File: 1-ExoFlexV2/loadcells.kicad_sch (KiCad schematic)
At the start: 50 parts, among them J70 3,3k, J71 3,3k, J72 0Ω, J73 0Ω, J74 0Ω, J75 0Ω, U13 INA823DR, U14 INA823DR, U15 INA823DR, U19 SN74LVC1G32DBVR, U20 SN74LVC1G32DBVR

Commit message: Schématisation terminée
- Schéma terminé
- Passage vers le PCB
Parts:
- C22, C23, C24, C25, C26, C27: renamed from C?; value * -> 10nF 10V X5R; footprint Capacitor_SMD:C_0805_2012Metric -> Capacitor_SMD:C_01005_0402Metric; DESCRIPTION (none) -> 10000 pF ±10% 10V Ceramic Capacitor X5R 01005 (0402 Metric); MANUFACTURER (none) -> Murata Electronics; NOTES (none) -> DO NOT POPULATE; PACKAGE (none) -> 01005 (0402 Metric); PART NUMBER (none) -> GRM022R61A103KE19L; TYPE (none) -> SMD
- J74: renamed from J70; value 3,3k -> Tulip Conn; footprint Connector_PinHeader_2.54mm:PinHeader_1x02_P2.54mm_Vertical -> Connector_PinSocket_2.54mm:PinSocket_1x02_P2.54mm_Vertical; DESCRIPTION (none) -> 2 Position Socket Connector 0.100" (2.54mm) Through Hole Go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; MANUFACTURER (none) -> Preci-Dip; PACKAGE (none) -> 2 POS 0.100" (2.54mm); PART NUMBER (none) -> 801-87-002-10-001101; TYPE (none) -> Through Hole
- J75: renamed from J71; value 3,3k -> Tulip Conn; footprint Connector_PinHeader_2.54mm:PinHeader_1x02_P2.54mm_Vertical -> Connector_PinSocket_2.54mm:PinSocket_1x02_P2.54mm_Vertical; DESCRIPTION (none) -> 2 Position Socket Connector 0.100" (2.54mm) Through Hole Go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; MANUFACTURER (none) -> Preci-Dip; PACKAGE (none) -> 2 POS 0.100" (2.54mm); PART NUMBER (none) -> 801-87-002-10-001101; TYPE (none) -> Through Hole
- J76: renamed from J72; value 0Ω -> Tulip Conn; footprint Connector_PinHeader_2.54mm:PinHeader_1x02_P2.54mm_Vertical -> Connector_PinSocket_2.54mm:PinSocket_1x02_P2.54mm_Vertical; DESCRIPTION (none) -> 2 Position Socket Connector 0.100" (2.54mm) Through Hole Go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; MANUFACTURER (none) -> Preci-Dip; PACKAGE (none) -> 2 POS 0.100" (2.54mm); PART NUMBER (none) -> 801-87-002-10-001101; TYPE (none) -> Through Hole
- J77: renamed from J73; value 0Ω -> Tulip Conn; footprint Connector_PinHeader_2.54mm:PinHeader_1x02_P2.54mm_Vertical -> Connector_PinSocket_2.54mm:PinSocket_1x02_P2.54mm_Vertical; DESCRIPTION (none) -> 2 Position Socket Connector 0.100" (2.54mm) Through Hole Go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; MANUFACTURER (none) -> Preci-Dip; PACKAGE (none) -> 2 POS 0.100" (2.54mm); PART NUMBER (none) -> 801-87-002-10-001101; TYPE (none) -> Through Hole
- J78: renamed from J74; value 0Ω -> Tulip Conn; footprint Connector_PinHeader_2.54mm:PinHeader_1x02_P2.54mm_Vertical -> Connector_PinSocket_2.54mm:PinSocket_1x02_P2.54mm_Vertical; DESCRIPTION (none) -> 2 Position Socket Connector 0.100" (2.54mm) Through Hole Go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; MANUFACTURER (none) -> Preci-Dip; PACKAGE (none) -> 2 POS 0.100" (2.54mm); PART NUMBER (none) -> 801-87-002-10-001101; TYPE (none) -> Through Hole
- J79: renamed from J75; value 0Ω -> Tulip Conn; footprint Connector_PinHeader_2.54mm:PinHeader_1x02_P2.54mm_Vertical -> Connector_PinSocket_2.54mm:PinSocket_1x02_P2.54mm_Vertical; DESCRIPTION (none) -> 2 Position Socket Connector 0.100" (2.54mm) Through Hole Go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; MANUFACTURER (none) -> Preci-Dip; PACKAGE (none) -> 2 POS 0.100" (2.54mm); PART NUMBER (none) -> 801-87-002-10-001101; TYPE (none) -> Through Hole
- J80, J81, J82, J83, J84, J85: renamed from J?; value Jmp -> Jumper; footprint (none) -> Connector_PinSocket_2.54mm:PinSocket_1x03_P2.54mm_Vertical; DESCRIPTION (none) -> CONN HEADER VERT 3POS 2.54MM; MANUFACTURER (none) -> Würth Elektronik; PACKAGE (none) -> Square 0.100" (2.54mm); PART NUMBER (none) -> 61300311121; TYPE (none) -> Through Hole
- R59: renamed from R37; value 910k -> 910k 0,1% 1/8W; DESCRIPTION (none) -> 910 kOhms ±0.1% 0.125W, 1/8W Chip Resistor 0805 (2012 Metri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; MANUFACTURER (none) -> Panasonic Electronic Components; PACKAGE (none) -> 0805 (2012 Metric); PART NUMBER (none) -> ERA-6AEB914V; TYPE (none) -> SMD
- R60, R66: renamed from R?; value 910k -> 910k 0,1% 1/8W; DESCRIPTION (none) -> 910 kOhms ±0.1% 0.125W, 1/8W Chip Resistor 0805 (2012 Metri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; MANUFACTURER (none) -> Panasonic Electronic Components; PACKAGE (none) -> 0805 (2012 Metric); PART NUMBER (none) -> ERA-6AEB914V; TYPE (none) -> SMD
- R61, R62, R63, R64, R65, R67: renamed from R?; DESCRIPTION (none) -> 0 Ohms Jumper Chip Resistor 0805 (2012 Metric) Automotive A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; MANUFACTURER (none) -> Panasonic Electronic Components; PACKAGE (none) -> 0805 (2012 Metric); PART NUMBER (none) -> ERJ-6GEY0R00V; TYPE (none) -> SMD
- R68, R69, R70: renamed from R?; value 1k -> 1k 1% 1/10W; footprint Resistor_SMD:R_0805_2012Metric -> Resistor_SMD:R_0402_1005Metric; DESCRIPTION (none) -> 1 kOhms ±1% 0.1W, 1/10W Chip Resistor 0402 (1005 Metric) Au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; MANUFACTURER (none) -> Panasonic Electronic Components; PACKAGE (none) -> 0402 (1005 Metric); PART NUMBER (none) -> ERJ-2RKF1001X; TYPE (none) -> SMD
- R71, R72, R73, R74, R75, R76: renamed from R?; value 100k -> 100k 5% 1/8W; DESCRIPTION (none) -> 100 kOhms ±5% 0.125W, 1/8W Chip Resistor 0805 (2012 Metric)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; MANUFACTURER (none) -> Panasonic Electronic Components; PACKAGE (none) -> 0805 (2012 Metric); PART NUMBER (none) -> ERJ-6GEYJ104V; TYPE (none) -> SMD
- RV15: renamed from RV1; value 402Ω -> Trim 1k; DESCRIPTION (none) -> Trimmer 1k 0,5W PC PIN TOP; MANUFACTURER (none) -> Bourns Inc.; PACKAGE (none) -> Rectangular - 0.275" x 0.260" Face; PART NUMBER (none) -> 3362P-1-102LF; TYPE (none) -> Through Hole
- RV16: renamed from RV2; value 402Ω -> Trim 1k; DESCRIPTION (none) -> Trimmer 1k 0,5W PC PIN TOP; MANUFACTURER (none) -> Bourns Inc.; PACKAGE (none) -> Rectangular - 0.275" x 0.260" Face; PART NUMBER (none) -> 3362P-1-102LF; TYPE (none) -> Through Hole
- RV17: renamed from RV3; value 402Ω -> Trim 1k; DESCRIPTION (none) -> Trimmer 1k 0,5W PC PIN TOP; MANUFACTURER (none) -> Bourns Inc.; PACKAGE (none) -> Rectangular - 0.275" x 0.260" Face; PART NUMBER (none) -> 3362P-1-102LF; TYPE (none) -> Through Hole
- RV18, RV19, RV20: renamed from RV?; value 523Ω -> Trim 1k; DESCRIPTION (none) -> Trimmer 1k 0,5W PC PIN TOP; MANUFACTURER (none) -> Bourns Inc.; PACKAGE (none) -> Rectangular - 0.275" x 0.260" Face; PART NUMBER (none) -> 3362P-1-102LF; TYPE (none) -> Through Hole
- U25: renamed from U13; value INA823DR -> INST OP-AMP; DESCRIPTION (none) -> Instrumentation Amplifier 1 Circuit 8-SOIC; MANUFACTURER (none) -> Texas Instruments; PACKAGE (none) -> 8-SOIC (0.154", 3.90mm Width); PART NUMBER (none) -> INA823DR; TYPE (none) -> SMD
- U26: renamed from U14; value INA823DR -> INST OP-AMP; DESCRIPTION (none) -> Instrumentation Amplifier 1 Circuit 8-SOIC; MANUFACTURER (none) -> Texas Instruments; PACKAGE (none) -> 8-SOIC (0.154", 3.90mm Width); PART NUMBER (none) -> INA823DR; TYPE (none) -> SMD
- U27: renamed from U15; value INA823DR -> INST OP-AMP; DESCRIPTION (none) -> Instrumentation Amplifier 1 Circuit 8-SOIC; MANUFACTURER (none) -> Texas Instruments; PACKAGE (none) -> 8-SOIC (0.154", 3.90mm Width); PART NUMBER (none) -> INA823DR; TYPE (none) -> SMD
- U28, U29, U30: renamed from U?; value LM393DGKR -> COMP; footprint DGK8 -> FootPrint:DGK8; DESCRIPTION (none) -> Comparator General Purpose Open-Collector, Rail-to-Rail 8-V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; MANUFACTURER (none) -> Texas Instruments; PACKAGE (none) -> 8-TSSOP, 8-MSOP (0.118", 3.00mm Width); PART NUMBER (none) -> LM393DGKR; TYPE (none) -> SMD
- U31: renamed from U19; value SN74LVC1G32DBVR -> OR Gate; DESCRIPTION (none) -> OR Gate IC 1 Channel SOT-23-5; MANUFACTURER (none) -> Texas Instruments; PACKAGE (none) -> SC-74A, SOT-753; PART NUMBER (none) -> SN74LVC1G32DBVR; TYPE (none) -> SMD
- U32: renamed from U20; value SN74LVC1G32DBVR -> OR Gate; DESCRIPTION (none) -> OR Gate IC 1 Channel SOT-23-5; MANUFACTURER (none) -> Texas Instruments; PACKAGE (none) -> SC-74A, SOT-753; PART NUMBER (none) -> SN74LVC1G32DBVR; TYPE (none) -> SMD
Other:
- note added: "3,3kΩ"
- note added: "3xComp : 5VA @ 77,4mA 2xOrGate : 5V @ 64,02mA 3xPot10k : 5VA @ 30mA 3xLimit : 5VA @ 60mA 3x910k : 5VA @ 0,016mA 6x100k : 5VA @ 0,3mA 3xPot523 : 5VA @ 30mA 3xAmInst : ±5VA @ 150,9 Total current : 5V @ 69mA 5VA @ 357mA -5VA @ 150,9mA"
- note added: "402Ω"
- note added: "523Ω"
- note removed: "3xComp : 5VA @ 24,5mA 2xOrGate : 5V @ 64,02mA 3xInstAmp : ±5VA @ 150,9mA 3xPot10k : 5VA @ 1,5mA 3xLim10,2k : 5VA @ 1,47mA 3x200k : 5V @ 0,075mA 3x910k: 5VA @ 0,016mA Total current : 5VA @ 180mA -5VA @ 152mA 5V @150,02mA"
- moved on the sheet: C22, C26, C27, J78, J79, J83, R61, R66, R67, R73

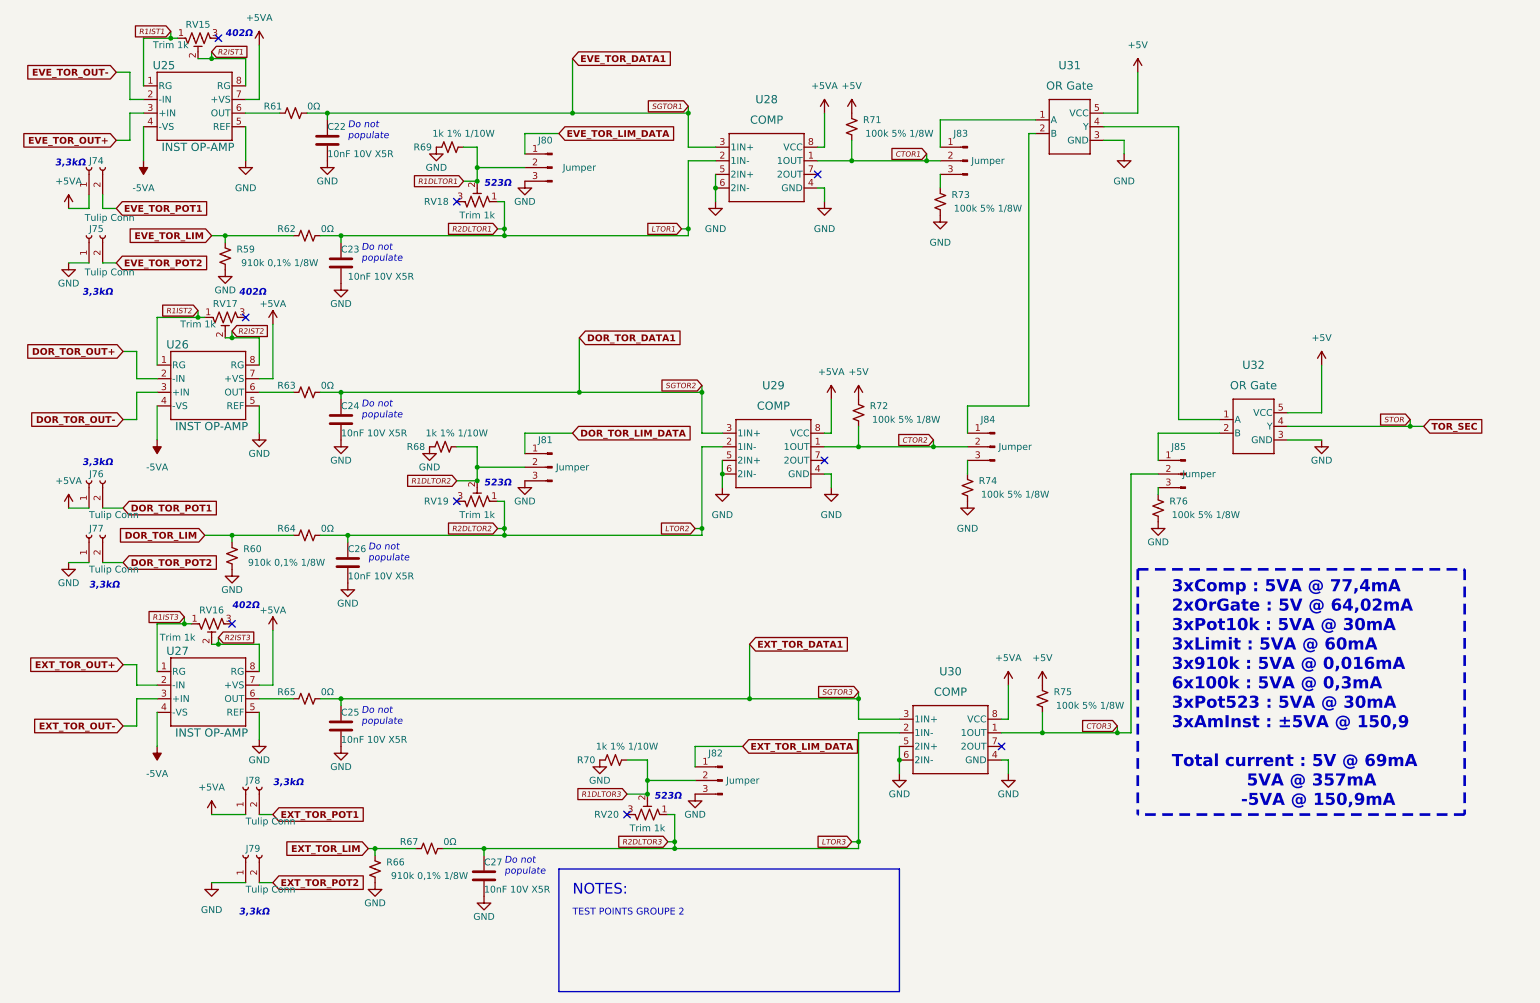
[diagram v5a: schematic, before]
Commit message: Finalisation 3
- Changement des régulateur de tension
- Retrait de test point inutile
- Changement de jumper mal positionner
- Ajout de Mounting holes et fiducial
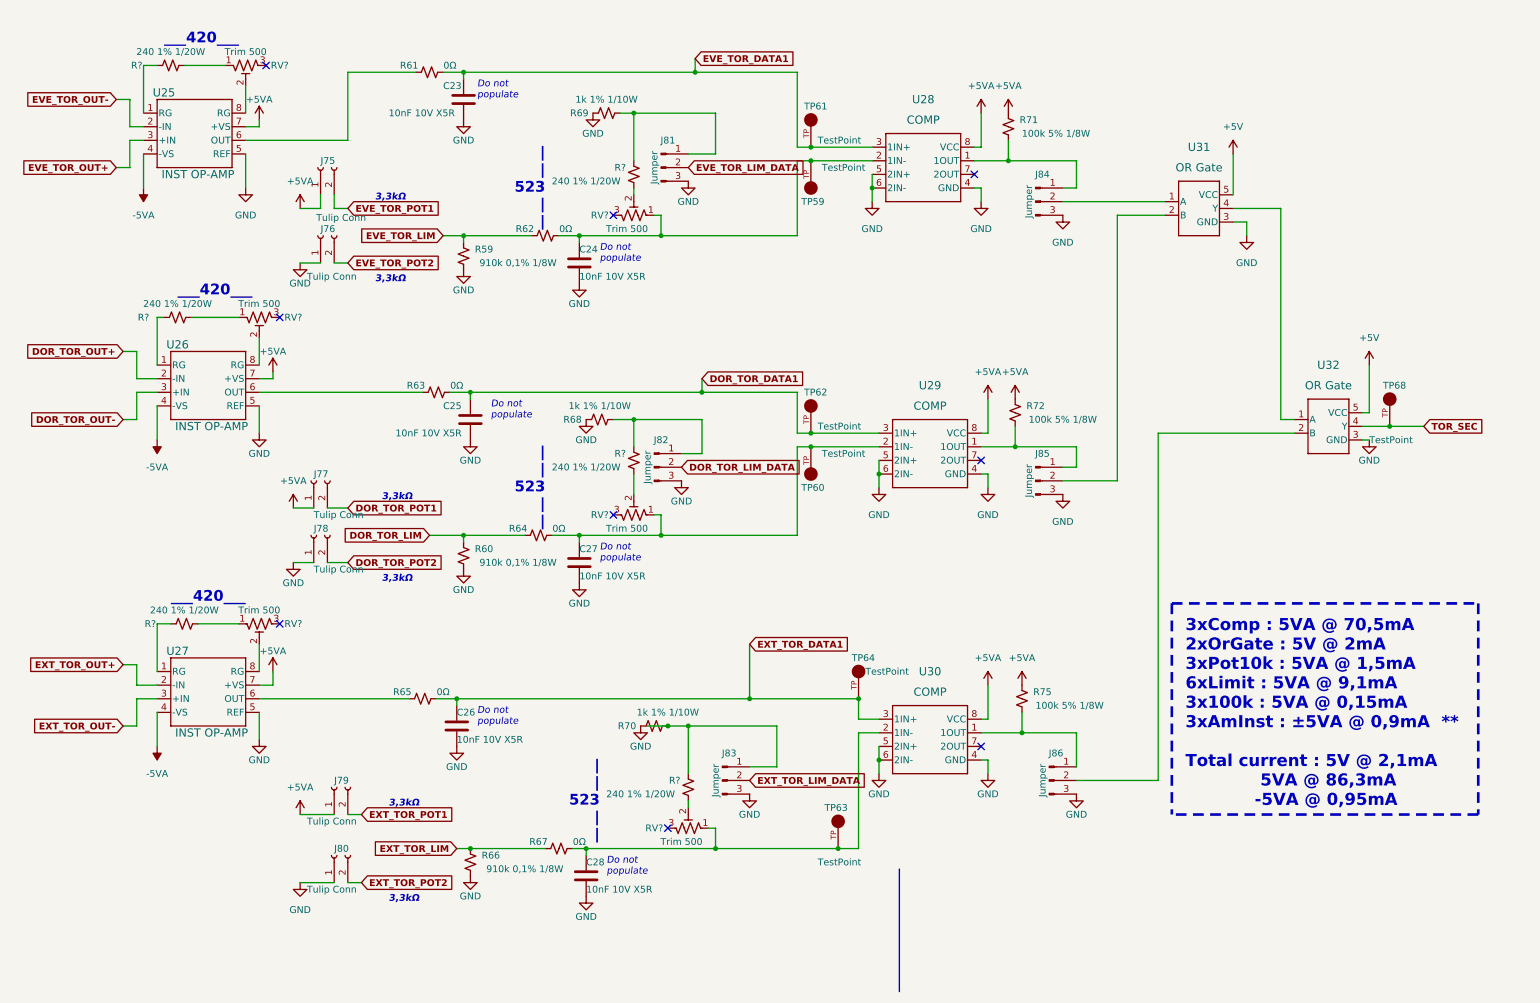
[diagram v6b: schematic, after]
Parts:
- removed C22: 10nF 10V X5R, Capacitor_SMD:C_01005_0402Metric, symbol Device:C
- removed R73, R74, R76: 100k 5% 1/8W, Resistor_SMD:R_0805_2012Metric, symbol Device:R_Small_US
- removed RV15, RV16, RV17, RV18, RV19, RV20: Trim 1k, FootPrint:TRIM_3362P-1-102LF, symbol Device:R_Potentiometer_Trim_US
- added C28: 10nF 10V X5R, Capacitor_SMD:C_0603_1608Metric, symbol Device:C
- added R? (x6): 240 1% 1/20W, Resistor_SMD:R_0201_0603Metric, symbol Device:R_Small_US
- added RV? (x6): Trim 500, FootPrint:TRIM_3296W-1-501LF, symbol Device:R_Potentiometer_Trim_US
- added TP59, TP60, TP61, TP62, TP63, TP64, TP68: TestPoint, FootPrint:KEYSTONE_5005, symbol SymLib:5005
- C23, C24, C25, C26, C27: footprint Capacitor_SMD:C_01005_0402Metric -> Capacitor_SMD:C_0603_1608Metric; DESCRIPTION 10000 pF ±10% 10V Ceramic Capacitor X5R 01005 (0402 Metric) -> 10000 pF ±5% 10V Ceramic Capacitor U2J 0603 (1608 Metric); PACKAGE 01005 (0402 Metric) -> 0603 (1608 Metric); PART NUMBER GRM022R61A103KE19L -> GRM1857U1A103JA44D
- J81: renamed from J80; footprint Connector_PinSocket_2.54mm:PinSocket_1x03_P2.54mm_Vertical -> Connector_PinHeader_2.54mm:PinHeader_1x03_P2.54mm_Vertical
- J82: renamed from J81; footprint Connector_PinSocket_2.54mm:PinSocket_1x03_P2.54mm_Vertical -> Connector_PinHeader_2.54mm:PinHeader_1x03_P2.54mm_Vertical
- J83: renamed from J82; footprint Connector_PinSocket_2.54mm:PinSocket_1x03_P2.54mm_Vertical -> Connector_PinHeader_2.54mm:PinHeader_1x03_P2.54mm_Vertical
- J84: renamed from J83; footprint Connector_PinSocket_2.54mm:PinSocket_1x03_P2.54mm_Vertical -> Connector_PinHeader_2.54mm:PinHeader_1x03_P2.54mm_Vertical
- J85: renamed from J84; footprint Connector_PinSocket_2.54mm:PinSocket_1x03_P2.54mm_Vertical -> Connector_PinHeader_2.54mm:PinHeader_1x03_P2.54mm_Vertical
- J86: renamed from J85; footprint Connector_PinSocket_2.54mm:PinSocket_1x03_P2.54mm_Vertical -> Connector_PinHeader_2.54mm:PinHeader_1x03_P2.54mm_Vertical
- renumbered J74 to J75, J75 to J76, J76 to J77, J77 to J78, J78 to J79, J79 to J80
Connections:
- net +5V: no longer R71.1, R72.1, R75.1
- net +5VA: now also R71.1, R72.1, R75.1
- net DOR_TOR_DATA1: now also C25.1, TP62.TP; no longer C24.1
- net DOR_TOR_LIM_DATA: now also J82.2 (Pin_2); no longer J82.1 (Pin_1)
- net EVE_TOR_DATA1: now also C23.1, TP61.TP
- net EVE_TOR_LIM_DATA: now also J81.2 (Pin_2); no longer J81.1 (Pin_1)
- net EXT_TOR_DATA1: now also C26.1, TP64.TP; no longer C25.1
- net EXT_TOR_LIM_DATA: now also J83.2 (Pin_2); no longer J83.1 (Pin_1)
- net GND: now also J84.3 (Pin_3), J85.3 (Pin_3), J86.3 (Pin_3), C28.2
- net at J86.1 (Pin_1): now also R75.2, U30.1 (1OUT); no longer U32.2 (B)
- net at J84.1 (Pin_1): now also R71.2, U28.1 (1OUT); no longer U31.1 (A)
- net at J85.1 (Pin_1): now also R72.2, U29.1 (1OUT); no longer U31.2 (B)
- removed net CTOR1: J84.2 (Pin_2), R71.2, U28.1 (1OUT)
- removed net CTOR2: J85.2 (Pin_2), R72.2, U29.1 (1OUT)
- removed net CTOR3: J86.2 (Pin_2), R75.2, U30.1 (1OUT)
- net LTOR1: no longer names the net of R62.2, U28.2 (1IN-)
- net LTOR1: now also C24.1, RV?.1, TP59.TP; no longer C23.1
- net LTOR2: no longer names the net of R64.2, U29.2 (1IN-)
- net LTOR2: now also C27.1, RV?.1, TP60.TP; no longer C26.1
- net LTOR3: no longer names the net of R67.2, U30.2 (1IN-)
- net LTOR3: now also C28.1, RV?.1, TP63.TP; no longer C27.1
- net R1DLTOR1: no longer names the net of R69.2
- net R1DLTOR1: now also J81.1 (Pin_1), R?.2; no longer J81.2 (Pin_2)
- net R1DLTOR2: no longer names the net of R68.2
- net R1DLTOR2: now also J82.1 (Pin_1), R?.2; no longer J82.2 (Pin_2)
- net R1DLTOR3: no longer names the net of R70.2
- net R1DLTOR3: now also J83.1 (Pin_1), R?.2; no longer J83.2 (Pin_2)
- net R1IST1: no longer names the net of U25.1 (RG)
- net R1IST1: now also R?.2
- net R1IST2: no longer names the net of U26.1 (RG)
- net R1IST2: now also R?.2
- net R1IST3: no longer names the net of U27.1 (RG)
- net R1IST3: now also R?.2
- net R2IST1: no longer names the net of U25.8 (RG)
- net R2IST1: now also RV?.2
- net R2IST2: no longer names the net of U26.8 (RG)
- net R2IST2: now also RV?.2
- net R2IST3: no longer names the net of U27.8 (RG)
- net R2IST3: now also RV?.2
- net STOR renamed TOR_SEC
- net TOR_SEC: now also TP68.TP
- new net: R?.1, RV?.2 (x3)
- new net: R?.1, RV?.1 (x3)
- new net: J86.2 (Pin_2), U32.2 (B)
- new net: J84.2 (Pin_2), U31.1 (A)
- new net: J85.2 (Pin_2), U31.2 (B)
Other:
- note added: "3xComp : 5VA @ 70,5mA 2xOrGate : 5V @ 2mA 3xPot10k : 5VA @ 1,5mA 6xLimit : 5VA @ 9,1mA 3x100k : 5VA @ 0,15mA 3xAmInst : ±5VA @ 0,9mA ** Total current : 5V @ 2,1mA 5VA @ 86,3mA -5VA @ 0,95mA"
- note added: "___420___"
- note added: "| | 523 | |"
- note removed: "3xComp : 5VA @ 77,4mA 2xOrGate : 5V @ 64,02mA 3xPot10k : 5VA @ 30mA 3xLimit : 5VA @ 60mA 3x910k : 5VA @ 0,016mA 6x100k : 5VA @ 0,3mA 3xPot523 : 5VA @ 30mA 3xAmInst : ±5VA @ 150,9 Total current : 5V @ 69mA 5VA @ 357mA -5VA @ 150,9mA"
- note removed: "402Ω"
- note removed: "523Ω"
- note removed: "NOTES:"
- note removed: "TEST POINTS GROUPE 2"
- moved on the sheet: J75, J76, J77, J78, J79, J80, J81, J82, J83, J84, J85, J86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
